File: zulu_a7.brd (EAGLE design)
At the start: 61 x 25.4 mm, 169 parts, among them J1 Pmod 2x6, Q1 12MHz 25ppm (FPGA + FT2232HQ), Q3 MBT3904DW1T1, U1 XC7A35T-1CPG236C, U10 93LC46BT-I/SN, U2 FT2232HQ USB-UART/JTAG Bridge, U3 AS4C32M16SB-6TIN, U4 W25Q128JVSIQ, U8 LTC3569EUDC#TRPBF, X1 Molex 105017-0001 Micro-USB-B

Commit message: Split R1, R2 and R4 into eleven discretes; one part left parked
R1 and R2 to 0201, R4 to 0402, as agreed. The arrays fitted NOWHERE -- a
742C083 needs 3.55 x 3.35 and the largest free square on this board was 2.9 x
2.9 front, 2.1 x 2.1 back -- so they were not short of a good spot, they were
short of any spot.

FIVE OF THE SIXTEEN ELEMENTS WERE NEVER CONNECTED. R1 used 2 of 4, R2 used 3 of
4, R4 used 6 of 8. Three arrays were holding 25.4 mm2 of a board with no room
in order to deliver eleven resistors. That is the real find; the size change is
secondary.

THE SYMBOL DID NOT CHANGE, WHICH IS WHY NO WIRE MOVED. R1NV0, the symbol the
arrays drew their elements with, has its pins 10.16 mm apart; R-US_SMALL has
them 5.08. Swapping to the discrete symbol would have pulled both pins 2.54 mm
inward on all eleven and stranded every net that touched them. So R1NV0 is
copied into rcl and a new deviceset R-WIDE hangs the R0201 and R0402 packages
off it. Each instance keeps its x, y and rotation; only the part behind it
changed. Net membership is identical, checked pin by pin against the old gates.

  R1.A -> R1   R1.B -> R3                       4.7k pull-ups/downs, 0201
  R2.A -> R2   R2.B -> R6   R2.D -> R7          4.7k flash pull-ups, 0201
  R4.A -> R4   R4.B -> R8   R4.C -> R9
  R4.F -> R36  R4.G -> R37  R4.H -> R38         100R JTAG series, 0402

R4 stayed 0402 on purpose. Contention through 100R is 109 mW from an ideal
source and 30-50 mW once the drivers' own impedance is counted; that is 60-100 %
of an 0201 and 48-80 % of an 0402. The 741X163 it replaces is a 1/16 W part, so
0402 keeps the rating the design had.

RES8 went with it, and 741X163, 742C163, 743C163, 744C163 and SOCKED-16 with
that -- 335 lines. RES4 stays: R34 is still a 4-pack.

Parked real parts 3 -> 1. 171 placed. Only R90 is left, a 10k pull-up on TDI,
and a pull-up is the least position-critical thing on the board.

Placement is uneven and worth knowing: R9 landed 4.3 mm from U1 and R38 7.3,
but the 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
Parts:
- added R3, R6, R7: 4.7K, rcl:R0201
- added R36, R37, R38, R8, R9: 100, rcl:R0402
- R1, R2: device ctambe:742C083 -> rcl:R0201
- R4: device ctambe:741X163 -> rcl:R0402
- moved R90 61.3 mm to (3.00, -17.6), flipped to the top, turned to 0 degrees
- moved R4 60.8 mm to (59.8, 18.2), turned to 90 degrees
- moved R2 53.3 mm to (50.7, 6.84), flipped to the bottom
- moved R1 39.8 mm to (47.1, 6.84), flipped to the bottom
- moved L6 16.2 mm to (38.2, 20.6), turned to 90 degrees
- moved R94 15.7 mm to (37.0, 20.7)
- moved R93 9.99 mm to (37.0, 4.45), turned to 0 degrees
- moved R20 7.66 mm to (42.1, 10.0), turned to 90 degrees
- moved R21 6.55 mm to (50.7, 10.0), turned to 90 degrees
- moved L7 6.31 mm to (31.9, 24.3), turned to 0 degrees
- moved R89 6.01 mm to (59.5, 12.2), flipped to the bottom
- moved R92 3.00 mm to (59.5, 15.2)
- moved R22 3.00 mm to (42.1, 13.0)
- moved R23 3.00 mm to (50.7, 13.0)
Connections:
- net DONE: now also R38.1; no longer R4.8
- net FLASH-CS#: now also R7.1; no longer R2.4
- net FLASH-D03: now also R6.1; no longer R2.2
- net FPGA-DONE: now also R38.2; no longer R4.9
- net FPGA-TCK: now also R36.2; no longer R4.11
- net FPGA-TDI: now also R8.2; no longer R4.15
- net FPGA-TDO: now also R37.2; no longer R4.10
- net FPGA-TMS: now also R4.2; no longer R4.16
- net GND: now also R3.2; no longer R1.7
- net PROG#: now also R9.1; no longer R4.3
- net RST#: now also R3.1, R9.2; no longer R1.2, R4.14
- net TCK: now also R36.1; no longer R4.6
- net TDI: now also R8.1; no longer R4.2
- net TDO: now also R37.1; no longer R4.7
- net VCC3V3: now also R1.2, R2.2, R6.2, R7.2; no longer R1.8, R2.5, R2.7, R2.8
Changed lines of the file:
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@@
 <element name="R34" library="ctambe" package="742C083" value="4.7K" x="2.9" y="21.45" rot="MR0"/>
 <element name="R35" library="rcl" package="R0402" value="4.7K" x="2.898" y="6.02" rot="MR0"/>
-<element name="R2" library="ctambe" package="742C083" value="4.7K" x="2.8" y="-16.5"/>
 <element name="U1" library="ctambe" package="XC7A35T-CPG236" value="XC7A35T-1CPG236C" x="42" y="16.74"/>
 <element name="R10" library="rcl" package="R0201" value="2.32K" x="26.594" y="8.1"/>
@@
 <element name="JP3" library="pinhead" package="1X03-NOSILK" value="JTAG TCK/TMS/GND" x="56.5" y="21.68"/>
 <element name="JP4" library="pinhead" package="1X03-NOSILK" value="JTAG TDI/TDO/3V3" x="56.5" y="3.72"/>
-<element name="R4" library="ctambe" package="741X163" value="100" x="10" y="-16.7"/>
 <element name="R5" library="rcl" package="R0603" value="5.1K" x="37.174" y="3.14"/>
-<element name="R1" library="ctambe" package="742C083" value="4.7K" x="14.8" y="-16.5"/>
+<element name="R1" library="rcl" package="R0201" value="4.7K" x="47.086" y="6.84" rot="MR0"/>
+<element name="R3" library="rcl" package="R0201" value="4.7K" x="48.882" y="6.84" rot="MR0"/>
+<element name="R2" library="rcl" package="R0201" value="4.7K" x="50.678" y="6.84" rot="MR0"/>
+<element name="R6" library="rcl" package="R0201" value="4.7K" x="41.698" y="14.832" rot="MR0"/>
+<element name="R7" library="rcl" package="R0201" value="4.7K" x="41.698" y="15.432" rot="MR0"/>
+<element name="R4" library="rcl" package="R0402" value="100" x="59.79" y="18.178" rot="R90"/>
+<element name="R8" library="rcl" package="R0402" value="100" x="59.5098" y="6.176" rot="MR90"/>
+<element name="R9" library="rcl" package="R0402" value="100" x="46.298" y="16.44" rot="MR0"/>
+<element name="R36" library="rcl" package="R0402" value="100" x="59.5098" y="18.178" rot="MR90"/>
+<element name="R37" library="rcl" package="R0402" value="100" x="59.5098" y="9.172" rot="MR90"/>
+<element name="R38" library="rcl" package="R0402" value="100" x="49.294" y="16.44" rot="MR0"/>
 <element name="U8" library="ctambe" package="LTC3569-QFN20" value="LTC3569EUDC#TRPBF" x="12.5" y="7.44" rot="MR0"/>
 <element name="D1" library="ctambe" package="SOD123" value="PMEG2020EJ,115" x="15.45" y="6.518" rot="MR90"/>
@@
 <element name="L4" library="ctambe" package="IND0603" value="FB 600R@100MHz" x="32.845" y="20.79" rot="MR0"/>
 <element name="L5" library="ctambe" package="IND0603" value="FB 600R@100MHz" x="23.896" y="22.36" rot="MR0"/>
-<element name="L6" library="ctambe" package="IND0603" value="FB 600R@100MHz" x="36.9" y="4.45" rot="MR0"/>
-<element name="L7" library="ctambe" package="IND0603" value="FB 600R@100MHz" x="37.045" y="20.63" rot="MR90"/>
+<element name="L6" library="ctambe" package="IND0603" value="FB 600R@100MHz" x="38.245" y="20.63" rot="MR90"/>
+<element name="L7" library="ctambe" package="IND0603" value="FB 600R@100MHz" x="31.9" y="24.284" rot="MR0"/>
 <element name="C123" library="rcl" package="C0402" value="100nF" x="49.75" y="7.89" rot="MR0"/>
 <element name="C124" library="rcl" package="C0402" value="470nF" x="43.15" y="16.49" rot="MR0"/>
 <element name="R18" library="rcl" package="R0402" value="12K 1%" x="29.732" y="4.45" rot="MR0"/>
 <element name="R19" library="rcl" package="R0402" value="10K" x="32.728" y="4.45" rot="MR0"/>
-<element name="R20" library="rcl" package="R0402" value="1K" x="46.298" y="16.44" rot="MR0"/>
-<element name="R21" library="rcl" package="R0402" value="1K" x="49.294" y="16.44" rot="MR0"/>
-<element name="R22" library="rcl" package="R0402" value="1K" x="42.1" y="10.038" rot="MR90"/>
-<element name="R23" library="rcl" package="R0402" value="1K" x="50.7" y="10.038" rot="MR90"/>
+<element name="R20" library="rcl" package="R0402" value="1K" x="42.1" y="10.038" rot="MR90"/>
+<element name="R21" library="rcl" package="R0402" value="1K" x="50.7" y="10.038" rot="MR90"/>
+<element name="R22" library="rcl" package="R0402" value="1K" x="42.1" y="13.034" rot="MR90"/>
+<element name="R23" library="rcl" package="R0402" value="1K" x="50.7" y="13.034" rot="MR90"/>
 <element name="C139" library="rcl" package="C0402" value="3.3uF" x="35.7" y="17.933"/>
 <element name="C39" library="rcl" package="C0402" value="3.3uF" x="36.234" y="18.58" rot="MR0"/>
@@
 <element name="R85" library="rcl" package="R0402" value="10K" x="15.65" y="13.364" rot="MR90"/>
 <element name="R86" library="rcl" package="R0402" value="10K" x="15.65" y="16.36" rot="MR90"/>
-<element name="R89" library="rcl" package="R0402" value="10K" x="59.79" y="18.178" rot="R90"/>
-<element name="R90" library="rcl" package="R0402" value="10K" x="59.5098" y="6.176" rot="MR90"/>
+<element name="R89" library="rcl" package="R0402" value="10K" x="59.5098" y="12.178" rot="MR90"/>
+<element name="R90" library="rcl" package="R0402" value="10K" x="3" y="-17.55"/>
 <element name="R91" library="rcl" package="R0402" value="10K" x="30.573" y="3.933"/>
-<element name="R92" library="rcl" package="R0402" value="10K" x="59.5098" y="18.178" rot="MR90"/>
-<element name="R93" library="rcl" package="R0402" value="10K" x="42.1" y="13.034" rot="MR90"/>
-<element name="R94" library="rcl" package="R0402" value="10K" x="50.7" y="13.034" rot="MR90"/>
+<element name="R92" library="rcl" package="R0402" value="10K" x="59.5098" y="15.174" rot="MR90"/>
+<element name="R93" library="rcl" package="R0402" value="10K" x="36.998" y="4.45" rot="MR0"/>
+<element name="R94" library="rcl" package="R0402" value="10K" x="37.045" y="20.728" rot="MR90"/>
 <element name="LD0" library="ctambe" package="VS-NRD8" value="VS NRD8" x="24.85" y="10.885"/>
 <element name="LD1" library="ctambe" package="LED0603" value="LED" x="24.95" y="12.585"/>
@@
 <contactref element="Q1" pad="1"/>
 <contactref element="Q1" pad="4"/>
-<contactref element="R1" pad="8"/>
+<contactref element="R1" pad="2"/>
 <contactref element="R100" pad="2"/>
 <contactref element="R19" pad="2"/>
-<contactref element="R2" pad="8"/>
-<contactref element="R2" pad="7"/>
-<contactref element="R2" pad="5"/>
+<contactref element="R2" pad="2"/>
 <contactref element="R20" pad="2"/>
 <contactref element="R23" pad="1"/>
@@
 <contactref element="R34" pad="5"/>
 <contactref element="R35" pad="2"/>
+<contactref element="R6" pad="2"/>
+<contactref element="R7" pad="2"/>
 <contactref element="R71" pad="2"/>
 <contactref element="R77" pad="2"/>
@@
 <contactref element="Q3" pad="2"/>
 <contactref element="Q3" pad="3"/>
-<contactref element="R1" pad="7"/>
 <contactref element="R11" pad="1"/>
 <contactref element="R13" pad="2"/>
@@
 <contactref element="R21" pad="1"/>
 <contactref element="R22" pad="1"/>
+<contactref element="R3" pad="2"/>
 <contactref element="R5" pad="1"/>
 <contactref element="R66" pad="1"/>
@@
 </signal>
 <signal name="RST#">
-<contactref element="R1" pad="2"/>
-<contactref element="R4" pad="14"/>
+<contactref element="R3" pad="1"/>
+<contactref element="R9" pad="2"/>
 <contactref element="U1" pad="V10"/>
 <contactref element="X2" pad="24"/>
@@
 </signal>
 <signal name="FLASH-CS#">
-<contactref element="R2" pad="4"/>
+<contactref element="R7" pad="1"/>
 <contactref element="U1" pad="K19"/>
 <contactref element="U4" pad="1"/>
@@
 </signal>
 <signal name="FLASH-D03">
-<contactref element="R2" pad="2"/>
+<contactref element="R6" pad="1"/>
 <contactref element="U1" pad="F18"/>
 <contactref element="U4" pad="7"/>
@@
 </signal>
 <signal name="FPGA-TCK">
-<contactref element="R4" pad="11"/>
+<contactref element="R36" pad="2"/>
 <contactref element="R5" pad="2"/>
 <contactref element="U1" pad="C8"/>
 </signal>
 <signal name="FPGA-TMS">
-<contactref element="R4" pad="16"/>
+<contactref element="R4" pad="2"/>
 <contactref element="U1" pad="W9"/>
 </signal>
 <signal name="FPGA-TDI">
-<contactref element="R4" pad="15"/>
+<contactref element="R8" pad="2"/>
 <contactref element="U1" pad="W10"/>
 </signal>
 <signal name="FPGA-TDO">
-<contactref element="R4" pad="10"/>
+<contactref element="R37" pad="2"/>
 <contactref element="U1" pad="W8"/>
 </signal>
 <signal name="FPGA-DONE">
-<contactref element="R4" pad="9"/>
+<contactref element="R38" pad="2"/>
 <contactref element="U1" pad="U12"/>
 </signal>
 <signal name="TCK">
 <contactref element="JP3" pad="1"/>
-<contactref element="R4" pad="6"/>
+<contactref element="R36" pad="1"/>
 <contactref element="R89" pad="1"/>
 <contactref element="U2" pad="16"/>
@@
 <signal name="TDI">
 <contactref element="JP4" pad="1"/>
-<contactref element="R4" pad="2"/>
+<contactref element="R8" pad="1"/>
 <contactref element="R90" pad="1"/>
 <contactref element="U2" pad="17"/>
@@
 <signal name="TDO">
 <contactref element="JP4" pad="2"/>
-<contactref element="R4" pad="7"/>
+<contactref element="R37" pad="1"/>
 <contactref element="R91" pad="1"/>
 <contactref element="U2" pad="18"/>
 </signal>
 <signal name="PROG#">
-<contactref element="R4" pad="3"/>
+<contactref element="R9" pad="1"/>
 <contactref element="R99" pad="1"/>
 <contactref element="U2" pad="21"/>
@@
 <signal name="DONE">
 <contactref element="R100" pad="1"/>
-<contactref element="R4" pad="8"/>
+<contactref element="R38" pad="1"/>
 <contactref element="U2" pad="22"/>
 </signal>

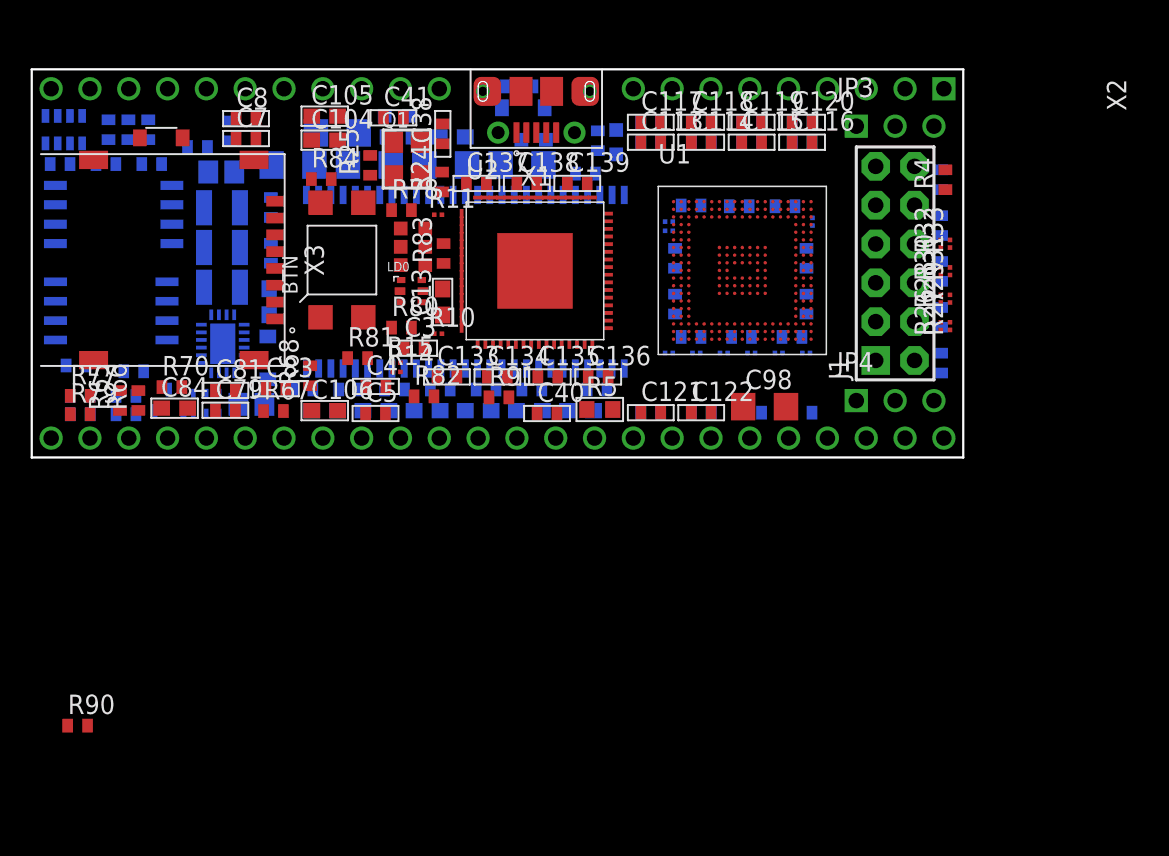
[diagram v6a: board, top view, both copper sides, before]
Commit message: The 22 HF decoupling caps go 0402 -> 0201, and the board is fully placed
Option A: package only, value untouched. New C0201 package in rcl on the same
land as R0201 -- C0402 and R0402 already share theirs, so the pair follows -- and
a C0201 device on C-US.

IT PUT THEM CLOSER, WHICH IS THE POINT. Distance from the ball centre goes
min 8.4 -> 5.1, median 9.3 -> 6.8, max 9.7 -> 10.9. The median moving 2.5 mm in
is worth more than the one outlier moving out: a bypass capacitor's loop is what
it costs you, and a smaller body reaches nearer the ball it serves. Lower ESL on
top of that is why Cmod A7 does it.

WHAT IT COSTS, RECORDED ON ALL 22 AS A NOTE RATHER THAN LEFT TO BE REDISCOVERED.
The 16 V GRM155R61C474KA88D becomes a 6.3 V 0201. On VCC3V3 that part sits at
52 % of rating, where DC bias typically takes 60-75 % of the capacitance against
15-25 % for the 16 V 0402. The BOM value does not change, so validate.py's UG483
count still reads 16/8/2 and passes -- it counts nominal values and cannot see
bias derating. Effective decoupling on the 3V3 rail is roughly half what it was.
That is the trade the ESL and the placement bought, and it should be checked
against Murata's bias curves before this is ordered, along with the MPN suffix.

The 4.7 uF and the 47 uF stay where they are. Not a judgement -- 0201 tops out
around 1 to 2.2 uF, so there is no part to convert them to.

C124 is untouched. It is the same GRM155R61C474KA88D and would have been swept
up by a global replace, but it is a 470 nF on FPGA CONNECT, not U1 decoupling on
sheet 7. An assertion on the MPN count caught it: 23 in the file, 22 on the sheet.

Every real part is now on the board. 172 placed, 0 parked -- the only things
below the outline are the four padless CC artwork blocks, which are parked by
design. check_board and validate 0 findings.

Co-Authored-By: Claude Opus 5 <noreply@anthropic.com>
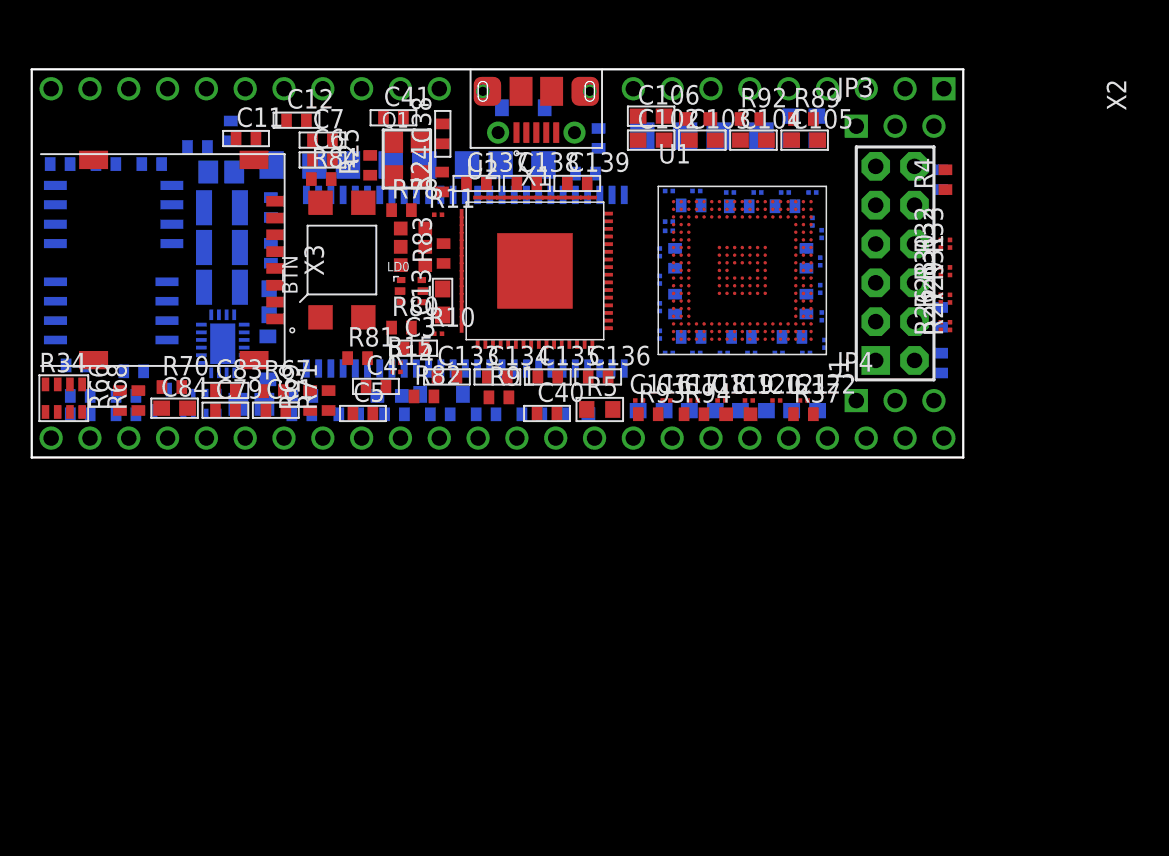
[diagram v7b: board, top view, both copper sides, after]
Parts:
- C107, C108, C109, C110, C111, C112, C113, C114, C115, C116, C117, C118, C119, C120, C121, C122, C89, C90, C91, C92, C95, C96: device rcl:C0402 -> rcl:C0201
- moved R90 62.5 mm to (59.5, 9.17), flipped to the bottom, turned to 90 degrees
- moved C105 31.4 mm to (50.6, 20.8)
- moved C106 28.8 mm to (40.5, 22.3)
- moved C104 28.1 mm to (47.2, 20.8)
- moved C87 26.4 mm to (50.5, 20.8)
- moved C140 26.4 mm to (46.4, 21.0)
- moved D3 24.9 mm to (26.8, 4.13), flipped to the bottom
- moved C8 23.1 mm to (37.1, 20.9), flipped to the bottom, turned to 90 degrees
- moved C88 23.0 mm to (50.5, 22.3)
- moved C101 21.4 mm to (50.6, 3.06)
- moved C94 21.4 mm to (40.5, 3.06)
- moved C99 21.4 mm to (43.9, 3.06)
- moved C100 21.4 mm to (47.2, 3.06)
- moved C116 20.0 mm to (39.7, 3.73)
- moved L6 19.5 mm to (46.2, 2.83), flipped to the top, turned to 0 degrees
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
